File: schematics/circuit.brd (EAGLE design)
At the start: 100 x 80 mm, 47 parts, among them IC1 TLC271D, IC2 TLC271D, U1 AD5241BRU1M-REEL7AD5241BRZ1M, X1 87758-1816

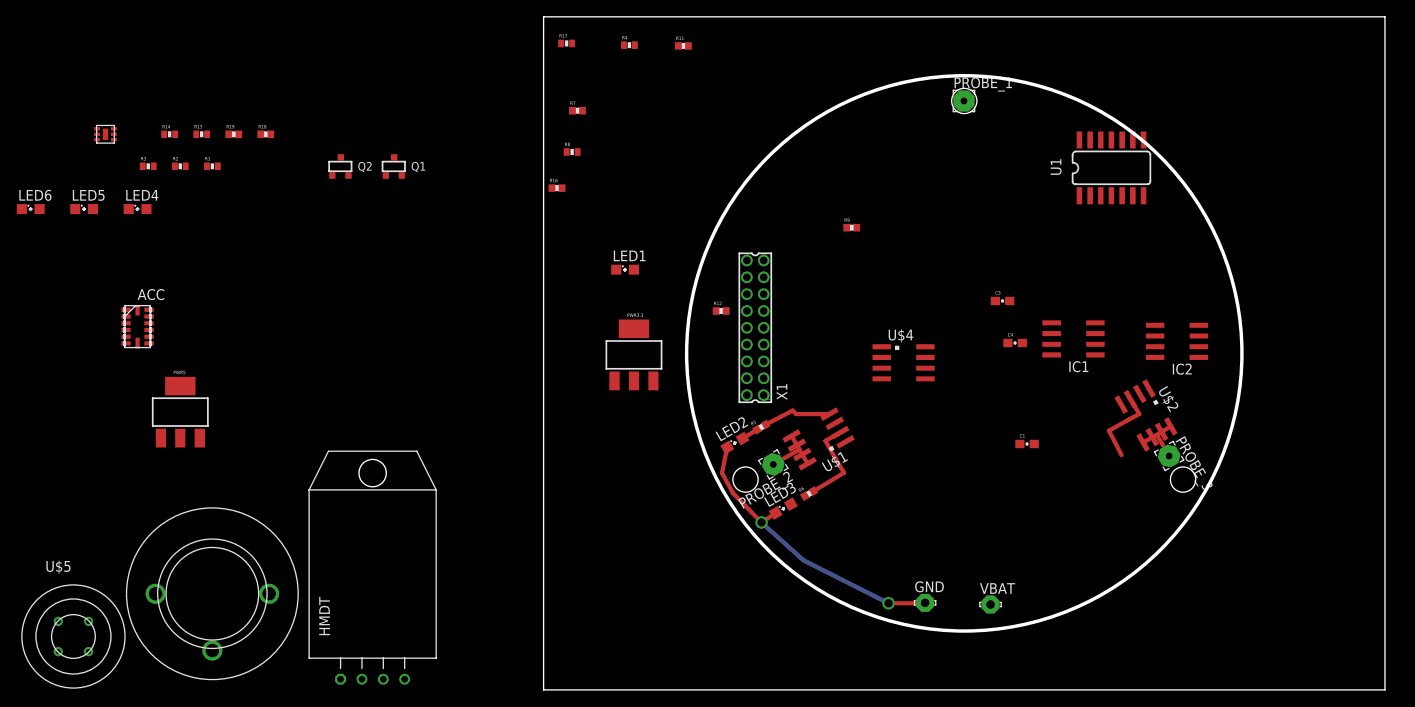
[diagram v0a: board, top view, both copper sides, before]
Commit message: Добавлена плата
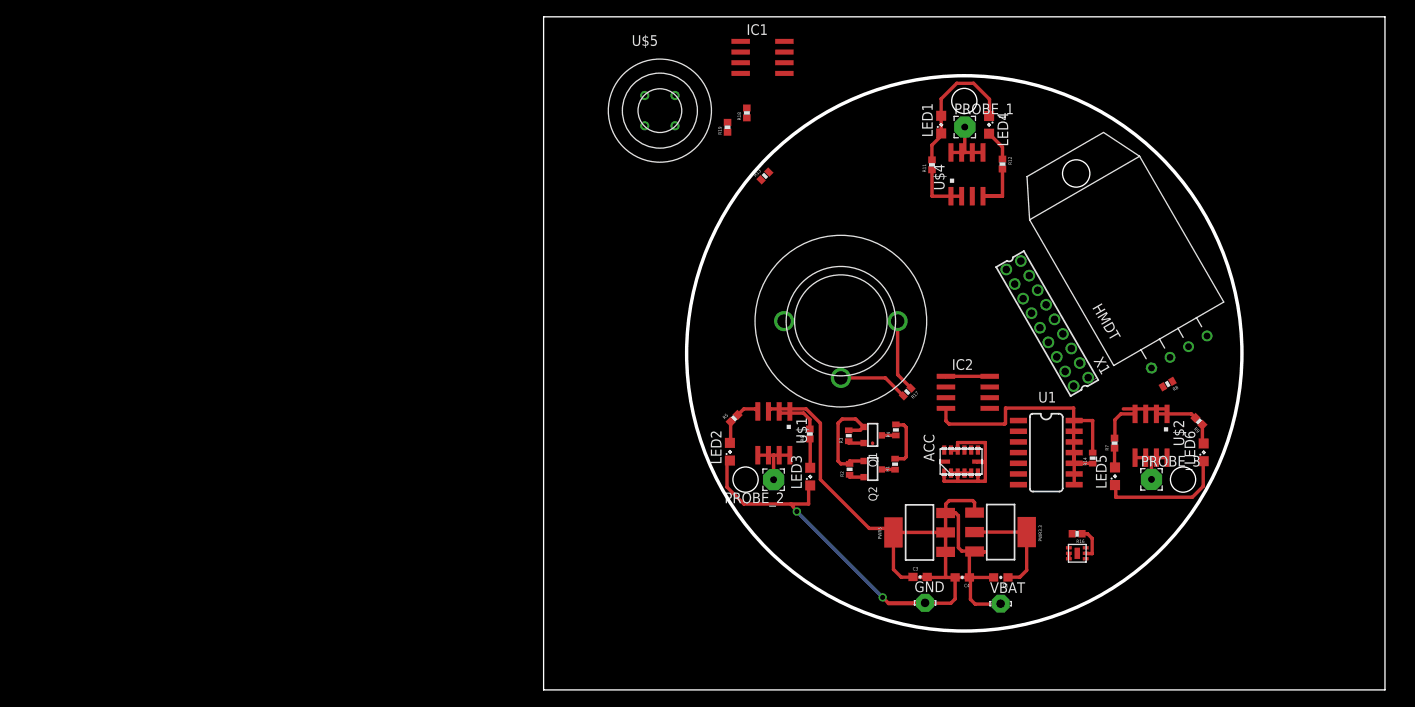
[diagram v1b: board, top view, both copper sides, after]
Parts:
- moved LED6 142.4 mm to (78.5, 28.2), turned to 90 degrees
- moved LED5 126.6 mm to (67.9, 25.4), turned to 90 degrees
- moved U$3 125.8 mm to (63.4, 16.2)
- moved R14 116.3 mm to (65.3, 27.6), turned to 90 degrees
- moved HMDT 103.5 mm to (75.6, 40.2), turned to 30 degrees
- moved LED4 101.7 mm to (53.0, 67.2), turned to 270 degrees
- moved ACC 99.2 mm to (49.6, 27.1), turned to 90 degrees
- moved U$5 93.6 mm to (13.8, 68.8)
- moved R3 89.2 mm to (36.3, 30.2), turned to 90 degrees
- moved PWR5 89.0 mm to (44.7, 18.7), turned to 90 degrees
- moved R1 88.5 mm to (41.8, 26.8), turned to 90 degrees
- moved R2 87.3 mm to (36.4, 26.2), turned to 90 degrees
- moved U$6 81.4 mm to (35.3, 43.8)
- moved R8 76.0 mm to (74.2, 36.4), turned to 210 degrees
- moved R7 75.1 mm to (67.9, 29.3), turned to 90 degrees
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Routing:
- net GND: track 35.1 -> 121.8 mm
- net 5V: track 9.42 -> 62.0 mm
- net 3.3V: track 0.00 -> 45.4 mm
- net VBAT: track 0.00 -> 20.4 mm
- net N$4: track 0.00 -> 18.1 mm
- net N$7: track 0.00 -> 7.84 mm
- net N$6: track 0.00 -> 7.84 mm
- net N$16: track 0.00 -> 7.21 mm
- net N$28: track 0.00 -> 6.01 mm
- net N$5: track 0.00 -> 5.89 mm
- net N$17: track 10.6 -> 5.20 mm
- net N$11: track 8.18 -> 2.83 mm
- net N$13: track 0.00 -> 4.89 mm
- net N$9: track 0.00 -> 4.84 mm
- net N$19: track 0.00 -> 4.03 mm
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
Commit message: В схему добавлены пережигатели и выключатель + обновлена плата + начата работа с отдельной платой для gps
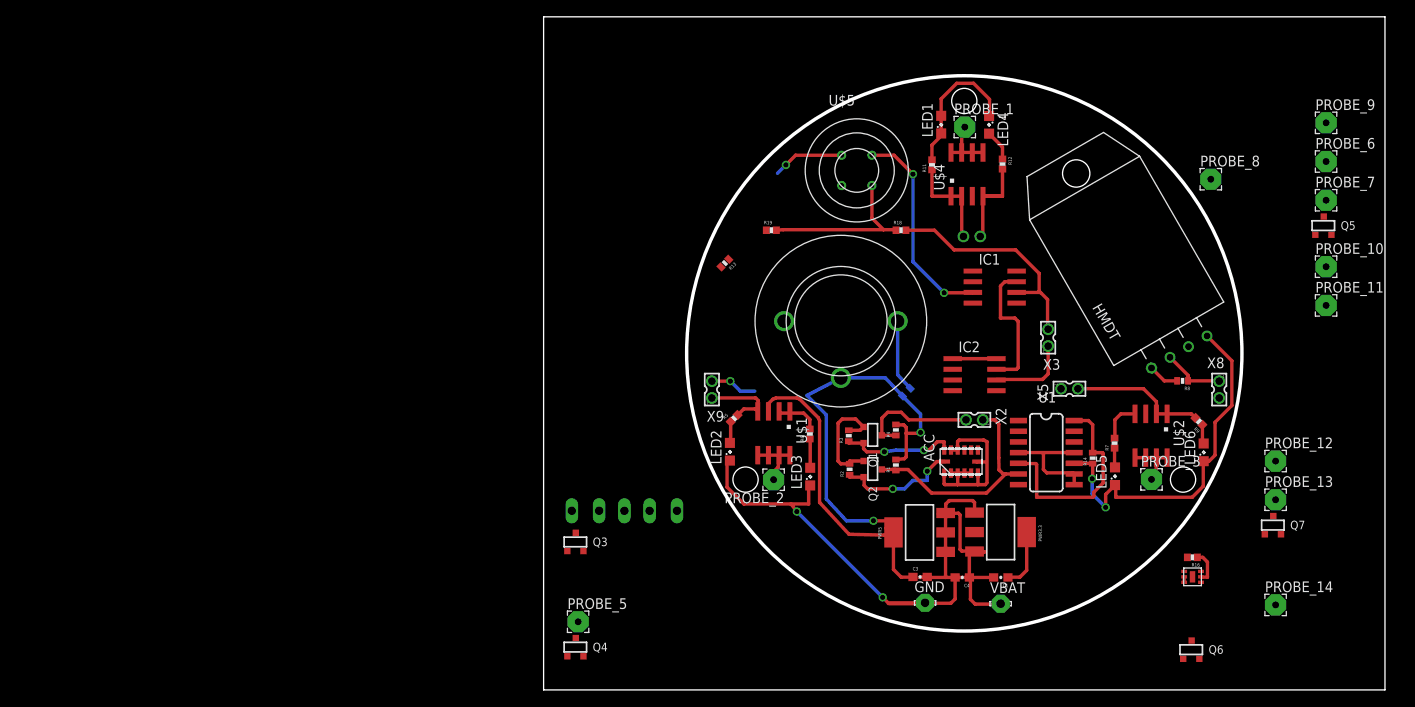
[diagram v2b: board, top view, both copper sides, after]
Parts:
- removed X1: 87758-1816, con-molex:87758-1816
- added PROBE_10, PROBE_11, PROBE_12, PROBE_13, PROBE_14, PROBE_5, PROBE_6, PROBE_7, PROBE_8, PROBE_9: (no value), wirepad:2,54/0,8
- added Q3, Q4, Q5, Q6, Q7: (no value), elements:SOT-23
- added U$9: SS-8, elements:SS-8
- added X2, X3, X4, X5, X8, X9: 87758-0216, con-molex:87758-0216
- moved IC1 38.8 mm to (53.6, 47.9)
- moved U$5 24.5 mm to (37.2, 61.8)
- moved R18 23.0 mm to (42.5, 54.6), turned to 0 degrees
- moved R16 14.0 mm to (77.1, 15.8)
- moved U$3 14.0 mm to (77.1, 13.4)
- moved R19 13.3 mm to (27.1, 54.6), turned to 0 degrees
- moved R13 11.4 mm to (21.5, 50.7), turned to 225 degrees
- moved IC2 2.25 mm to (51.2, 37.5)
- moved R8 1.81 mm to (75.9, 36.7), turned to 180 degrees
- moved R1 0.14 mm to (41.9, 26.7)
- moved R17 0.10 mm to (43.1, 35.4), flipped to the bottom, turned to 315 degrees
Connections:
- new net N$18: PROBE_5.1, Q3.3
- new net N$23: PROBE_8.1, Q4.3
- new net N$25: PROBE_12.1
- new net N$27: PROBE_7.1, Q5.3
- new net N$29: PROBE_11.1, Q6.3
- new net N$30: PROBE_13.1, Q7.3
- new net N$31: PROBE_10.1
- new net N$32: PROBE_6.1
- new net N$33: U$9.P2, VBAT.MP
- new net N$34: PROBE_9.1
- net GND: now also Q3.2, Q4.2, Q5.2, Q6.2, Q7.2
- net N$11: now also X9.1; no longer X1.12
- net N$13: now also X5.1; no longer X1.16
- net N$17: now also X9.2; no longer X1.14
- net N$20: now also X3.1; no longer X1.9
- net N$24: now also X3.2; no longer X1.17
- net N$3: now also X8.1; no longer X1.2
- net N$6: now also X4.2; no longer X1.10
- net N$7: now also X4.1; no longer X1.8
- net N$9: now also X5.2; no longer X1.18
- net SCL_5V: now also X2.1; no longer X1.6
- net SDA_5V: now also X2.2; no longer X1.4
- net VBAT: now also PROBE_14.1, U$9.COM; no longer VBAT.MP
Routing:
- net 5V: track 62.0 -> 125.8 mm, vias 0 -> 2
- net N$24: track 0.00 -> 28.5 mm
- net SCL_5V: track 1.63 -> 27.1 mm
- net N$22: track 0.00 -> 24.9 mm, vias 0 -> 2
- net N$28: track 6.01 -> 25.5 mm
- net V+: track 0.00 -> 16.4 mm
- net SCL_3.3V: track 1.95 -> 14.8 mm, vias 0 -> 2
- net SDA_5V: track 1.68 -> 14.4 mm
- net SDA_3.3V: track 2.02 -> 13.8 mm, vias 0 -> 2
- net N$9: track 4.84 -> 16.3 mm
- net GND: track 121.8 -> 132.7 mm, vias 2 -> 5
- net N$20: track 0.00 -> 9.80 mm
- net N$3: track 0.00 -> 7.40 mm
- net N$11: track 2.83 -> 9.77 mm
- net N$17: track 5.20 -> 10.8 mm, vias 0 -> 1
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
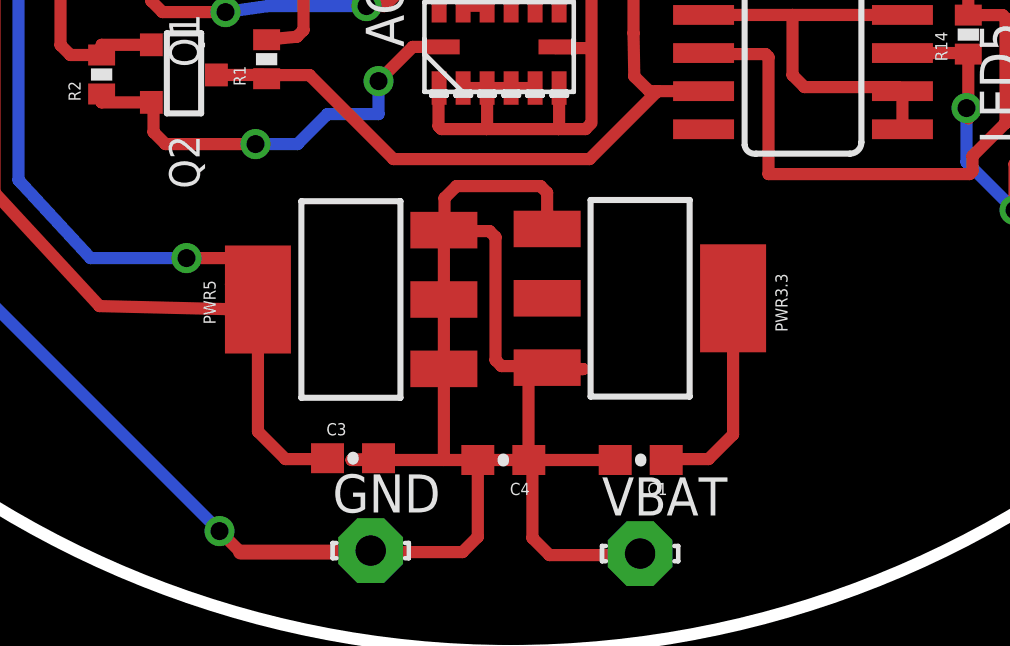
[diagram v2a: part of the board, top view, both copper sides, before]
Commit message: Исправил пару мелких ошибок на схеме. Вынес регуляторы напряжения из спаркфановской библиотеки в нашу - elements и правильно объединил им выводы. Исправил символ для TGS* датчика CO2. Все элементы обновил на схеме
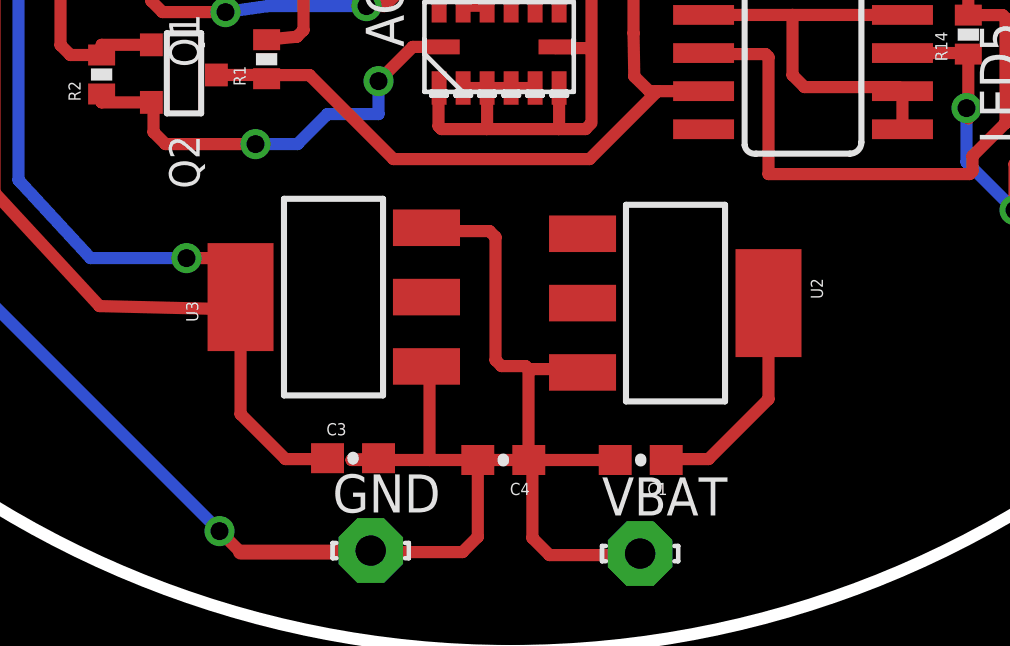
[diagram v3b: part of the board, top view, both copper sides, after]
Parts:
- removed PWR3.3, PWR5: (no value), SparkFun-PowerIC:SOT223
- added U2, U3: (no value), elements:SOT223
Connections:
- removed net HEAT-: U$5.4
- removed net N$31: PROBE_10.1
- removed net N$32: PROBE_6.1
- removed net N$34: PROBE_9.1
- net 3.3V: now also U2.2, U2.4; no longer PWR3.3.2, PWR3.3.4
- net 5V: now also U3.2, U3.4; no longer PWR5.2, PWR5.4
- net GND: now also U$5.4, U2.1, U3.1; no longer PWR3.3.1, PWR5.1
- net VBAT: now also PROBE_10.1, PROBE_6.1, PROBE_9.1, U2.3, U3.3; no longer PWR3.3.3, PWR5.3
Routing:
- net GND: track 132.7 -> 122.2 mm
- net 5V: track 125.8 -> 122.6 mm
- net VBAT: track 20.6 -> 18.5 mm

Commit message: Вышла на финишную прямую с основной платой Начата работа с платой gps
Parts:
- removed R16: 10, SparkFun-Resistors:0402-RES
- removed U$3: OPT3001, datchiki:OPT3001
- moved Q4 81.7 mm to (69.4, 53.8), flipped to the bottom, turned to 90 degrees
- moved PROBE_5 78.6 mm to (60.5, 62.9), flipped to the bottom
- moved Q3 77.9 mm to (67.2, 62.9), flipped to the bottom, turned to 270 degrees
- moved PROBE_9 54.4 mm to (67.6, 19.3)
- moved U$9 50.5 mm to (60.0, 21.3), flipped to the bottom
- moved PROBE_6 48.3 mm to (71.9, 19.3)
- moved PROBE_10 48.0 mm to (62.5, 13.3)
- moved PROBE_11 39.5 mm to (62.3, 20.8), flipped to the bottom
- moved PROBE_14 35.4 mm to (55.7, 26.6)
- moved PROBE_12 25.9 mm to (62.3, 19.3)
- moved PROBE_7 25.3 mm to (69.5, 48.8), flipped to the bottom
- moved PROBE_13 25.1 mm to (62.2, 26.7), flipped to the bottom
- moved Q7 20.3 mm to (67.7, 26.7), flipped to the bottom, turned to 270 degrees
- moved Q5 18.3 mm to (75.5, 48.9), flipped to the bottom, turned to 270 degrees
- moved Q6 16.1 mm to (67.2, 17.6), flipped to the bottom, turned to 180 degrees
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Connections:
- removed net N$19: R16.1, U$3.5
- removed net N$25: PROBE_12.1
- net 3.3V: no longer R16.2, U$3.1
- net GND: no longer U$3.2, U$3.3
- net SCL_3.3V: no longer U$3.4
- net SDA_3.3V: no longer U$3.6
- net VBAT: now also PROBE_12.1
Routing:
- net GND: track 122.2 -> 365.3 mm, vias 5 -> 24
- net 5V: track 122.6 -> 212.5 mm, vias 2 -> 12
- net N$5: track 0.66 -> 89.4 mm, vias 0 -> 5
- net 3.3V: track 45.2 -> 105.2 mm, vias 0 -> 4
- net VBAT: track 18.5 -> 62.1 mm, vias 0 -> 2
- net N$33: track 0.00 -> 18.1 mm, vias 0 -> 1
- net N$24: track 28.5 -> 13.2 mm
- net N$26: track 0.00 -> 15.0 mm, vias 0 -> 2
- net N$17: track 10.8 -> 20.7 mm, vias 1 -> 4
- net N$29: track 0.00 -> 8.85 mm
- net SDA_5V: track 14.4 -> 22.2 mm
- net N$18: track 0.00 -> 5.66 mm
- net N$23: track 0.00 -> 5.06 mm
- net N$27: track 0.00 -> 5.01 mm
- net N$9: track 16.3 -> 11.3 mm
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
